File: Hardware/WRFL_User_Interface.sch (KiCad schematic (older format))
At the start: 13 parts, among them P15 1x8_2_54_FEM, P16 2x3_2_54_RA_MALE, Q3 SI1012CR, SW1 TSA12110, SW2 EN11-HSB, SW3 TSA12110, U9 S25FL216K0PMFI040

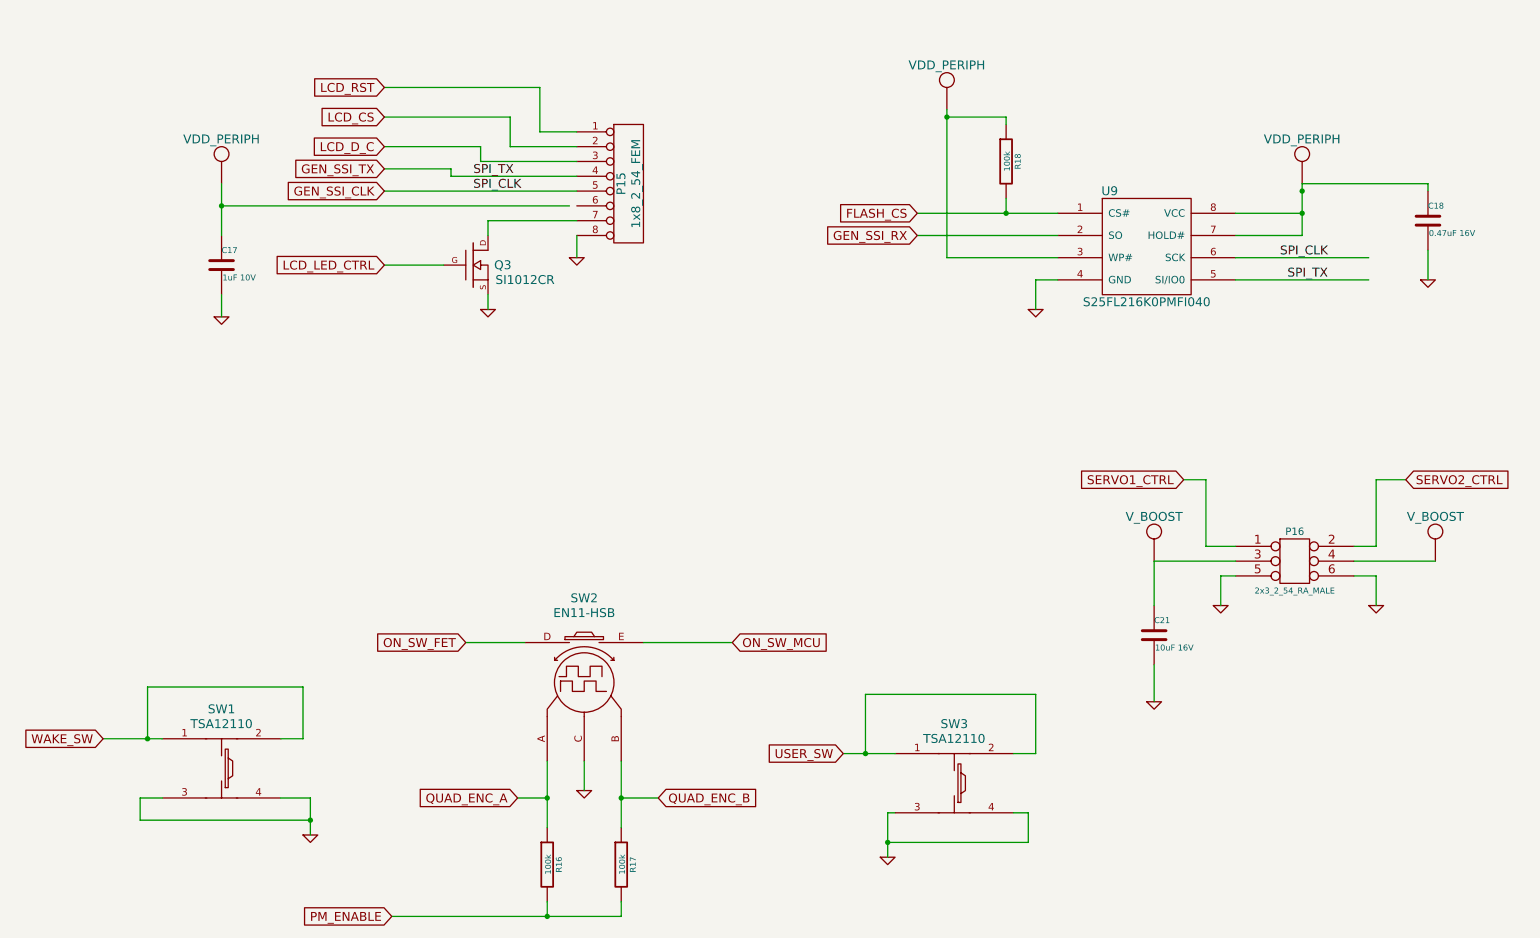
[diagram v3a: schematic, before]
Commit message: Schematics update
Bluetooth sheet added
LCD specific symbol
power management sheet rearrangement
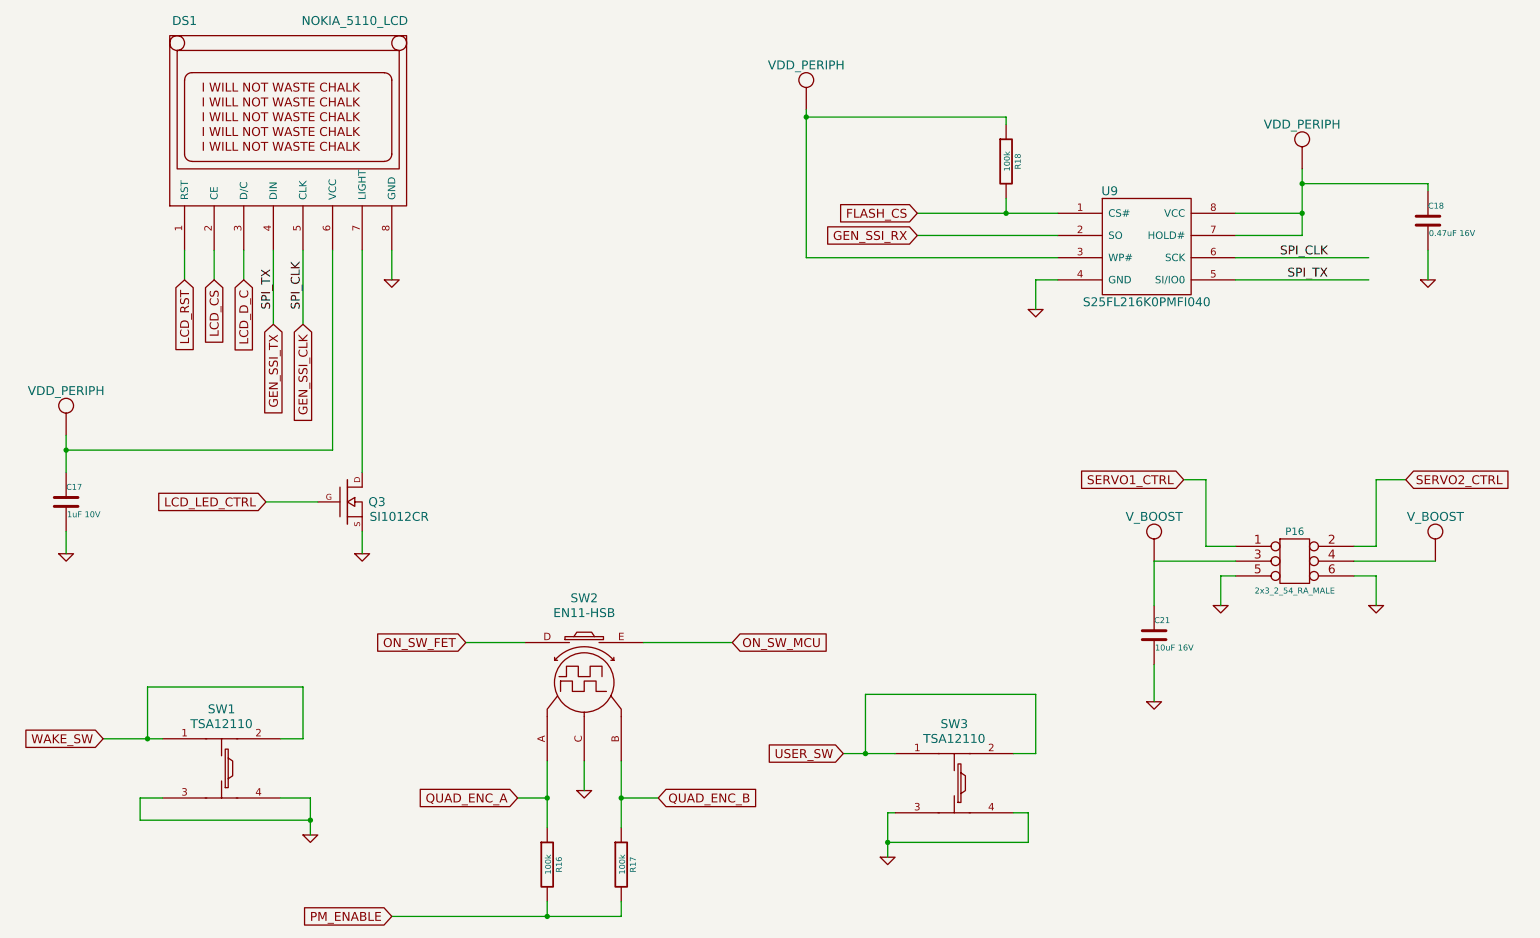
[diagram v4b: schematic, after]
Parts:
- removed P15: 1x8_2_54_FEM, symbol CONN_8
- added DS1: NOKIA_5110_LCD, symbol NOKIA_5110_LCD
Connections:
- wire segments 82 -> 74
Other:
- moved on the sheet: C17, Q3
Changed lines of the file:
@@
-EESchema Schematic File Version 2  date Monday, October 07, 2013 12:52:48 PM
+EESchema Schematic File Version 2  date 10/11/2013 1:57:23 AM
 LIBS:power
 LIBS:device
@@
 $Descr A4 11693 8268
 encoding utf-8
-Sheet 4 5
+Sheet 4 6
 Title ""
-Date "7 oct 2013"
+Date "10 oct 2013"
 Rev ""
 Comp "Nightmechanic"
@@
 $EndComp
 $Comp
-L CONN_8 P15
-U 1 1 5251E176
-P 4750 1850
-F 0 "P15" V 4700 1850 60  0000 C CNN
-F 1 "1x8_2_54_FEM" V 4800 1850 60  0000 C CNN
-F 2 "" H 4750 1850 60  0000 C CNN
-F 3 "" H 4750 1850 60  0000 C CNN
-	1    4750 1850
-	1    0    0    -1
-$EndComp
-$Comp
 L SI1012CR Q3
 U 1 1 5251E185
-P 3700 2400
-F 0 "Q3" H 3900 2400 60  0000 C CNN
-F 1 "SI1012CR" H 4050 2300 60  0000 C CNN
-F 2 "SC-75A" H 3700 2400 60  0001 C CNN
-F 3 "http://www.vishay.com/docs/67519/si1012cr.pdf" H 3650 2150 60  0001 C CNN
-	1    3700 2400
+P 2850 4000
+F 0 "Q3" H 3050 4000 60  0000 C CNN
+F 1 "SI1012CR" H 3200 3900 60  0000 C CNN
+F 2 "SC-75A" H 2850 4000 60  0001 C CNN
+F 3 "http://www.vishay.com/docs/67519/si1012cr.pdf" H 2800 3750 60  0001 C CNN
+	1    2850 4000
 	1    0    0    -1
 $EndComp
@@
 	1    0    0    -1
 $EndComp
-Text GLabel 3100 1200 0    60   Input ~ 0
+Text GLabel 1750 2500 3    60   Input ~ 0
 LCD_RST
-Text GLabel 3100 1400 0    60   Input ~ 0
+Text GLabel 1950 2500 3    60   Input ~ 0
 LCD_CS
-Text GLabel 3100 1600 0    60   Input ~ 0
+Text GLabel 2150 2500 3    60   Input ~ 0
 LCD_D_C
-Text GLabel 3100 1750 0    60   Input ~ 0
+Text GLabel 2350 2800 3    60   Input ~ 0
 GEN_SSI_TX
-Text GLabel 3100 1900 0    60   Input ~ 0
+Text GLabel 2550 2800 3    60   Input ~ 0
 GEN_SSI_CLK
 $Comp
-L VDD_PERIPH #U12
+L VDD_PERIPH #U13
 U 1 1 5251E2C5
-P 2000 1650
-F 0 "#U12" H 2000 1850 60  0001 C CNN
-F 1 "VDD_PERIPH" H 2000 1750 60  0000 C CNN
-F 2 "~" H 2000 1650 60  0000 C CNN
-F 3 "~" H 2000 1650 60  0000 C CNN
-	1    2000 1650
-	1    0    0    -1
-$EndComp
-$Comp
-L VDD_PERIPH #U14
+P 950 3350
+F 0 "#U13" H 950 3550 60  0001 C CNN
+F 1 "VDD_PERIPH" H 950 3450 60  0000 C CNN
+F 2 "~" H 950 3350 60  0000 C CNN
+F 3 "~" H 950 3350 60  0000 C CNN
+	1    950  3350
+	1    0    0    -1
+$EndComp
+$Comp
+L VDD_PERIPH #U16
 U 1 1 5251E301
-P 9300 1650
-F 0 "#U14" H 9300 1850 60  0001 C CNN
-F 1 "VDD_PERIPH" H 9300 1750 60  0000 C CNN
-F 2 "~" H 9300 1650 60  0000 C CNN
-F 3 "~" H 9300 1650 60  0000 C CNN
-	1    9300 1650
+P 9300 1550
+F 0 "#U16" H 9300 1750 60  0001 C CNN
+F 1 "VDD_PERIPH" H 9300 1650 60  0000 C CNN
+F 2 "~" H 9300 1550 60  0000 C CNN
+F 3 "~" H 9300 1550 60  0000 C CNN
+	1    9300 1550
 	1    0    0    -1
 $EndComp
@@
 L GND #PWR31
 U 1 1 5251E310
-P 2000 2750
-F 0 "#PWR31" H 2000 2750 30  0001 C CNN
-F 1 "GND" H 2000 2680 30  0001 C CNN
-F 2 "" H 2000 2750 60  0000 C CNN
-F 3 "" H 2000 2750 60  0000 C CNN
-	1    2000 2750
+P 950 4350
+F 0 "#PWR31" H 950 4350 30  0001 C CNN
+F 1 "GND" H 950 4280 30  0001 C CNN
+F 2 "" H 950 4350 60  0000 C CNN
+F 3 "" H 950 4350 60  0000 C CNN
+	1    950  4350
 	1    0    0    -1
 $EndComp
@@
 L GND #PWR34
 U 1 1 5251E34C
-P 4400 2350
-F 0 "#PWR34" H 4400 2350 30  0001 C CNN
-F 1 "GND" H 4400 2280 30  0001 C CNN
-F 2 "" H 4400 2350 60  0000 C CNN
-F 3 "" H 4400 2350 60  0000 C CNN
-	1    4400 2350
+P 3150 2500
+F 0 "#PWR34" H 3150 2500 30  0001 C CNN
+F 1 "GND" H 3150 2430 30  0001 C CNN
+F 2 "" H 3150 2500 60  0000 C CNN
+F 3 "" H 3150 2500 60  0000 C CNN
+	1    3150 2500
 	1    0    0    -1
 $EndComp
@@
 	1    0    0    -1
 $EndComp
-Wire Wire Line
-	3100 1200 4150 1200
-Wire Wire Line
-	4150 1200 4150 1500
-Wire Wire Line
-	4150 1500 4400 1500
-Wire Wire Line
-	3100 1400 3950 1400
-Wire Wire Line
-	3950 1400 3950 1600
-Wire Wire Line
-	3950 1600 4400 1600
-Wire Wire Line
-	3100 1600 3750 1600
-Wire Wire Line
-	3750 1600 3750 1700
-Wire Wire Line
-	3750 1700 4400 1700
-Wire Wire Line
-	3100 1750 3550 1750
-Wire Wire Line
-	3550 1750 3550 1800
-Wire Wire Line
-	3550 1800 4400 1800
-Wire Wire Line
-	4400 1900 3100 1900
-Wire Wire Line
-	4400 2200 4400 2350
 $Comp
 L GND #PWR33
 U 1 1 5251E3CC
-P 3800 2700
-F 0 "#PWR33" H 3800 2700 30  0001 C CNN
-F 1 "GND" H 3800 2630 30  0001 C CNN
-F 2 "" H 3800 2700 60  0000 C CNN
-F 3 "" H 3800 2700 60  0000 C CNN
-	1    3800 2700
-	1    0    0    -1
-$EndComp
-Wire Wire Line
-	3800 2600 3800 2700
-Wire Wire Line
-	4400 2100 3800 2100
-Wire Wire Line
-	3800 2100 3800 2200
+P 2950 4350
+F 0 "#PWR33" H 2950 4350 30  0001 C CNN
+F 1 "GND" H 2950 4280 30  0001 C CNN
+F 2 "" H 2950 4350 60  0000 C CNN
+F 3 "" H 2950 4350 60  0000 C CNN
+	1    2950 4350
+	1    0    0    -1
+$EndComp
 $Comp
 L C C17
 U 1 1 5251E3F3
-P 2000 2400
-F 0 "C17" H 2000 2500 40  0000 L CNN
-F 1 "1uF 10V" H 2006 2315 40  0000 L CNN
-F 2 "0805" H 2038 2250 30  0001 C CNN
-F 3 "~" H 2000 2400 60  0000 C CNN
-	1    2000 2400
-	1    0    0    -1
-$EndComp
-Wire Wire Line
-	2000 1850 2000 2200
-Wire Wire Line
-	2000 2600 2000 2750
-Wire Wire Line
-	2000 2000 4350 2000
-Connection ~ 2000 2000
-Text GLabel 3100 2400 0    60   Input ~ 0
+P 950 4000
+F 0 "C17" H 950 4100 40  0000 L CNN
+F 1 "1uF 10V" H 956 3915 40  0000 L CNN
+F 2 "0805" H 988 3850 30  0001 C CNN
+F 3 "~" H 950 4000 60  0000 C CNN
+	1    950  4000
+	1    0    0    -1
+$EndComp
+Wire Wire Line
+	950  4200 950  4350
+Text GLabel 2300 4000 0    60   Input ~ 0
 LCD_LED_CTRL
-Wire Wire Line
-	3500 2400 3100 2400
-Text Label 3700 1800 0    60   ~ 0
-SPI_TX
-Text Label 3700 1900 0    60   ~ 0
+Text Label 2550 2700 1    60   ~ 0
 SPI_CLK
 Wire Wire Line
@@
 SPI_TX
 Wire Wire Line
-	8850 2050 9300 2050
-Wire Wire Line
-	9300 1850 9300 2200
+	9300 2050 8850 2050
+Wire Wire Line
+	9300 1750 9300 2200
 Wire Wire Line
 	9300 2200 8850 2200
@@
 Wire Wire Line
 	10150 2300 10150 2500
-Connection ~ 9300 1900
-Wire Wire Line
-	9300 1850 10150 1850
 Wire Wire Line
 	10150 1850 10150 1900
 $Comp
-L VDD_PERIPH #U13
+L VDD_PERIPH #U14
 U 1 1 5251EAB9
-P 6900 1150
-F 0 "#U13" H 6900 1350 60  0001 C CNN
-F 1 "VDD_PERIPH" H 6900 1250 60  0000 C CNN
-F 2 "~" H 6900 1150 60  0000 C CNN
-F 3 "~" H 6900 1150 60  0000 C CNN
-	1    6900 1150
+P 5950 1150
+F 0 "#U14" H 5950 1350 60  0001 C CNN
+F 1 "VDD_PERIPH" H 5950 1250 60  0000 C CNN
+F 2 "~" H 5950 1150 60  0000 C CNN
+F 3 "~" H 5950 1150 60  0000 C CNN
+	1    5950 1150
 	1    0    0    -1
 $EndComp
@@
 	7300 2050 7300 1950
 Wire Wire Line
-	7300 1450 7300 1400
-Wire Wire Line
-	7300 1400 6900 1400
-Wire Wire Line
-	6900 1350 6900 2350
-Wire Wire Line
-	6900 2350 7650 2350
-Connection ~ 6900 1400
+	7300 1400 7300 1450
+Wire Wire Line
+	5950 1400 7300 1400
+Wire Wire Line
+	5950 2350 7650 2350
 Text GLabel 6700 2200 0    60   Input ~ 0
 GEN_SSI_RX
@@
 USER_SW
 Wire Wire Line
-	6550 5700 6200 5700
+	6200 5700 6550 5700
 Wire Wire Line
 	7350 5700 7500 5700
@@
 Connection ~ 6350 5700
 Wire Wire Line
-	1600 5600 1200 5600
+	1200 5600 1600 5600
 Wire Wire Line
 	4450 5750 4450 5950
@@
 	9800 4500 9800 4700
 $Comp
-L V_BOOST #U7
+L V_BOOST #U15
 U 1 1 52523B29
 P 8300 4200
-F 0 "#U7" H 8300 4400 60  0001 C CNN
+F 0 "#U15" H 8300 4400 60  0001 C CNN
 F 1 "V_BOOST" H 8300 4300 60  0000 C CNN
 F 2 "~" H 8300 4200 60  0000 C CNN
@@
 $EndComp
 $Comp
-L V_BOOST #U8
+L V_BOOST #U17
 U 1 1 52523B38
 P 10200 4200
-F 0 "#U8" H 10200 4400 60  0001 C CNN
+F 0 "#U17" H 10200 4400 60  0001 C CNN
 F 1 "V_BOOST" H 10200 4300 60  0000 C CNN
 F 2 "~" H 10200 4200 60  0000 C CNN
@@
 Wire Wire Line
 	8300 5100 8300 5350
+$Comp
+L NOKIA_5110_LCD DS1
+U 1 1 52572B07
+P 2450 1550
+F 0 "DS1" H 1750 2350 60  0000 C CNN
+F 1 "NOKIA_5110_LCD" H 2900 2350 60  0000 C CNN
+F 2 "" H 2300 1400 60  0000 C CNN
+F 3 "" H 2300 1400 60  0000 C CNN
+	1    2450 1550
+	1    0    0    -1
+$EndComp
+Wire Wire Line
+	2550 2300 2550 2800
+Wire Wire Line
+	2350 2800 2350 2300
+Wire Wire Line
+	2150 2300 2150 2500
+Wire Wire Line
+	1950 2500 1950 2300
+Wire Wire Line
+	1750 2300 1750 2500
+Text Label 2350 2700 1    60   ~ 0
+SPI_TX
+Wire Wire Line
+	2750 2300 2750 3650
+Wire Wire Line
+	2750 3650 950  3650
+Wire Wire Line
+	950  3550 950  3800
+Connection ~ 950  3650
+Wire Wire Line
+	2300 4000 2650 4000
+Wire Wire Line
+	3150 2300 3150 2500
+Wire Wire Line
+	2950 2300 2950 3800
+Wire Wire Line
+	2950 4200 2950 4350
+Wire Wire Line
+	5950 1350 5950 2350
+Connection ~ 5950 1400
+Wire Wire Line
+	10150 1850 9300 1850
+Connection ~ 9300 1850
 $EndSCHEMATC

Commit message: more changes
Changed BAS40 to BAT54C
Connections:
- net PM_ENABLE is gone; now on net VDD_PERIPH: R16.2, R17.2
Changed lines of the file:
@@
-EESchema Schematic File Version 2  date 10/11/2013 1:57:23 AM
+EESchema Schematic File Version 2  date Tuesday, October 15, 2013 09:37:22 AM
 LIBS:power
 LIBS:device
@@
 Sheet 4 6
 Title ""
-Date "10 oct 2013"
+Date "15 oct 2013"
 Rev ""
 Comp "Nightmechanic"
@@
 	1    0    0    -1
 $EndComp
-Text GLabel 1750 2500 3    60   Input ~ 0
+Text GLabel 1750 2800 3    60   Input ~ 0
 LCD_RST
-Text GLabel 1950 2500 3    60   Input ~ 0
+Text GLabel 1950 2800 3    60   Input ~ 0
 LCD_CS
-Text GLabel 2150 2500 3    60   Input ~ 0
+Text GLabel 2150 2800 3    60   Input ~ 0
 LCD_D_C
 Text GLabel 2350 2800 3    60   Input ~ 0
@@
 	9300 2050 8850 2050
 Wire Wire Line
-	9300 1750 9300 2200
+	9300 1750 9300 1850
+Wire Wire Line
+	9300 1850 9300 2050
+Wire Wire Line
+	9300 2050 9300 2200
 Wire Wire Line
 	9300 2200 8850 2200
@@
 $EndComp
 Wire Wire Line
-	6700 2050 7650 2050
+	6700 2050 7300 2050
+Wire Wire Line
+	7300 2050 7650 2050
 Wire Wire Line
 	7300 2050 7300 1950
@@
 	6550 6100 6500 6100
 Wire Wire Line
-	6500 6100 6500 6400
+	6500 6100 6500 6300
+Wire Wire Line
+	6500 6300 6500 6400
 Wire Wire Line
 	7350 6100 7450 6100
@@
 	2400 6000 2600 6000
 Wire Wire Line
-	2600 6000 2600 6250
+	2600 6000 2600 6150
+Wire Wire Line
+	2600 6150 2600 6250
 Wire Wire Line
 	2600 6150 1450 6150
@@
 Text GLabel 3650 4950 0    60   Input ~ 0
 ON_SW_FET
-Text GLabel 3150 6800 0    60   Input ~ 0
-PM_ENABLE
 Text GLabel 4000 6000 0    60   Input ~ 0
 QUAD_ENC_A
@@
 USER_SW
 Wire Wire Line
-	6200 5700 6550 5700
+	6200 5700 6350 5700
+Wire Wire Line
+	6350 5700 6550 5700
 Wire Wire Line
 	7350 5700 7500 5700
@@
 Connection ~ 6350 5700
 Wire Wire Line
-	1200 5600 1600 5600
+	1200 5600 1500 5600
+Wire Wire Line
+	1500 5600 1600 5600
 Wire Wire Line
 	4450 5750 4450 5950
 Wire Wire Line
-	4700 5750 4700 6200
+	4700 5750 4700 6000
+Wire Wire Line
+	4700 6000 4700 6200
 Wire Wire Line
 	4700 6000 4950 6000
 Wire Wire Line
-	4200 5750 4200 6200
+	4200 5750 4200 6000
+Wire Wire Line
+	4200 6000 4200 6200
 Wire Wire Line
 	4200 6000 4000 6000
@@
 Connection ~ 4700 6000
 Wire Wire Line
-	3150 6800 4700 6800
+	3150 6800 4200 6800
+Wire Wire Line
+	4200 6800 4700 6800
 Wire Wire Line
 	4700 6800 4700 6700
@@
 	2350 2800 2350 2300
 Wire Wire Line
-	2150 2300 2150 2500
-Wire Wire Line
-	1950 2500 1950 2300
-Wire Wire Line
-	1750 2300 1750 2500
+	2150 2300 2150 2800
+Wire Wire Line
+	1950 2800 1950 2300
+Wire Wire Line
+	1750 2300 1750 2800
 Text Label 2350 2700 1    60   ~ 0
 SPI_TX
@@
 	2750 3650 950  3650
 Wire Wire Line
-	950  3550 950  3800
+	950  3550 950  3650
+Wire Wire Line
+	950  3650 950  3800
 Connection ~ 950  3650
 Wire Wire Line
@@
 	2950 4200 2950 4350
 Wire Wire Line
-	5950 1350 5950 2350
+	5950 1350 5950 1400
+Wire Wire Line
+	5950 1400 5950 2350
 Connection ~ 5950 1400
 Wire Wire Line
 	10150 1850 9300 1850
 Connection ~ 9300 1850
+$Comp
+L VDD_PERIPH #U?
+U 1 1 525D7AAA
+P 3150 6600
+F 0 "#U?" H 3150 6800 60  0001 C CNN
+F 1 "VDD_PERIPH" H 3150 6700 60  0000 C CNN
+F 2 "~" H 3150 6600 60  0000 C CNN
+F 3 "~" H 3150 6600 60  0000 C CNN
+	1    3150 6600
+	1    0    0    -1
+$EndComp
 $EndSCHEMATC
